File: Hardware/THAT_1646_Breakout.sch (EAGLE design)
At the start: 20 parts, among them IC2 THAT1646, J2 OUTPUT, J6 CHASSIS

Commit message: Routed board.
Worked through initial checklist.
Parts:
- removed H5, H6, H7, H8: STAND-OFF, SparkFun-Electromechanical:STAND-OFF
- added FD1, FD2: FIDUCIALUFIDUCIAL, SparkFun-Aesthetics:FIDUCIALUFIDUCIAL
- added LOGO1, LOGO2: SFE_LOGO_NAME.1_INCH, SparkFun-Aesthetics:SFE_LOGO_NAME.1_INCH
- added LOGO3: SFE_LOGO_FLAME.2_INCH, SparkFun-Aesthetics:SFE_LOGO_FLAME.2_INCH
- added LOGO4, LOGO5: OSHW-LOGOS, SparkFun-Aesthetics:OSHW-LOGOS
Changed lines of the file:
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@@
 <part name="IC2" library="that-ics" deviceset="THAT1646" device="" value="THAT1646"/>
 <part name="GND3" library="SparkFun-Aesthetics" deviceset="GND" device=""/>
-<part name="H5" library="SparkFun-Electromechanical" deviceset="STAND-OFF" device=""/>
-<part name="H6" library="SparkFun-Electromechanical" deviceset="STAND-OFF" device=""/>
-<part name="H7" library="SparkFun-Electromechanical" deviceset="STAND-OFF" device=""/>
-<part name="H8" library="SparkFun-Electromechanical" deviceset="STAND-OFF" device=""/>
 <part name="L1" library="SparkFun-Passives" deviceset="INDUCTOR" device="0603" value="27uH"/>
 <part name="L2" library="SparkFun-Passives" deviceset="INDUCTOR" device="0603" value="27uH"/>
@@
 <part name="SUPPLY14" library="SparkFun-Aesthetics" deviceset="VCC" device=""/>
 <part name="J6" library="SparkFun-Connectors" deviceset="M02" device="1X02_NO_SILK" value="CHASSIS"/>
+<part name="FD1" library="SparkFun-Aesthetics" deviceset="FIDUCIAL" device="UFIDUCIAL"/>
+<part name="FD2" library="SparkFun-Aesthetics" deviceset="FIDUCIAL" device="UFIDUCIAL"/>
+<part name="LOGO1" library="SparkFun-Aesthetics" deviceset="SFE_LOGO_NAME" device=".1_INCH"/>
+<part name="LOGO2" library="SparkFun-Aesthetics" deviceset="SFE_LOGO_NAME" device=".1_INCH"/>
+<part name="LOGO3" library="SparkFun-Aesthetics" deviceset="SFE_LOGO_FLAME" device=".2_INCH"/>
+<part name="LOGO4" library="SparkFun-Aesthetics" deviceset="OSHW-LOGO" device="S"/>
+<part name="LOGO5" library="SparkFun-Aesthetics" deviceset="OSHW-LOGO" device="S"/>
 </parts>
 <sheets>
@@
 <instance part="IC2" gate="G$1" x="71.12" y="111.76"/>
 <instance part="GND3" gate="1" x="63.5" y="114.3"/>
-<instance part="H5" gate="G$1" x="233.68" y="33.02"/>
-<instance part="H6" gate="G$1" x="233.68" y="30.48"/>
-<instance part="H7" gate="G$1" x="236.22" y="33.02"/>
-<instance part="H8" gate="G$1" x="236.22" y="30.48"/>
 <instance part="L1" gate="G$1" x="147.32" y="147.32" rot="R90"/>
 <instance part="L2" gate="G$1" x="147.32" y="139.7" rot="R90"/>
@@
 <instance part="SUPPLY14" gate="G$1" x="43.18" y="129.54"/>
 <instance part="J6" gate="G$1" x="210.82" y="129.54" rot="R180"/>
+<instance part="FD1" gate="G$1" x="246.38" y="20.32"/>
+<instance part="FD2" gate="G$1" x="246.38" y="17.78"/>
+<instance part="LOGO1" gate="G$1" x="187.96" y="35.56"/>
+<instance part="LOGO2" gate="G$1" x="187.96" y="35.56"/>
+<instance part="LOGO3" gate="G$1" x="180.34" y="38.1"/>
+<instance part="LOGO4" gate="G$1" x="157.48" y="45.72"/>
+<instance part="LOGO5" gate="G$1" x="157.48" y="45.72"/>
 </instances>
 <busses>

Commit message: Post-review updates.
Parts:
- removed C11, C12: 10uf, that-ics:PANA-EEE-1EA100NP
- removed LOGO5: OSHW-LOGOS, SparkFun-Aesthetics:OSHW-LOGOS
- added C3, C4: 10uf NP, that-ics:PANA-EEE-1EA100NP
- added FD3, FD4: FIDUCIALUFIDUCIAL, SparkFun-Aesthetics:FIDUCIALUFIDUCIAL
- added J1: (no value), SparkFun-Connectors:M04NO_SILK_ALL_ROUND
- added J3: CHASSIS, SparkFun-Connectors:M021X02_NO_SILK
- added J4: SN, SparkFun-Connectors:M01PTH_NO_SILK_YES_STOP
- added LOGO6: SFE_LOGO_FLAME.2_INCH, SparkFun-Aesthetics:SFE_LOGO_FLAME.2_INCH
- J5: value (none) -> TN; device SparkFun-Connectors:M04NO_SILK_ALL_ROUND -> SparkFun-Connectors:M01PTH_NO_SILK_YES_STOP
- J6: value CHASSIS -> RN; device SparkFun-Connectors:M021X02_NO_SILK -> SparkFun-Connectors:M01PTH_NO_SILK_YES_STOP
- JP1: value JUMPER-PAD-2-NC_BY_TRACE -> GND-JOIN
- L1, L2: PROD_ID (none) -> NDUC-12579
- LOGO1, LOGO2: value SFE_LOGO_NAME.1_INCH -> OSHW-LOGOS; device SparkFun-Aesthetics:SFE_LOGO_NAME.1_INCH -> SparkFun-Aesthetics:OSHW-LOGOS
- LOGO4: value OSHW-LOGOS -> SFE_LOGO_NAME.1_INCH; device SparkFun-Aesthetics:OSHW-LOGOS -> SparkFun-Aesthetics:SFE_LOGO_NAME.1_INCH
- renumbered C10 to C2, C7 to C6, C8 to C5, C9 to C1, IC2 to IC1, JP2 to JP1
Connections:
- new net N$1: J2.RING-NORM, J6.1
- new net N$2: J2.TIP-NORM, J5.1
- new net N$3: J2.EARTH-NORM, J4.1
- net GND: now also J1.1; no longer J5.1
- net GND-ISO: now also J3.1, J3.2; no longer J6.1, J6.2
- net N$10: now also C3.2, D1.COM; no longer C11.-, D2.COM
- net N$11: now also C4.2, D2.COM; no longer C12.-, D1.COM
- net N$13: now also C4.1; no longer C12.+
- net N$14: now also C3.1; no longer C11.+
- net N$16: now also J1.4; no longer J5.4
- net VCC: now also J1.3; no longer J5.3
- net VNEG: now also J1.2; no longer J5.2
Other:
- moved on the sheet: D1, D2, J2

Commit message: Updates from engineering checklist.
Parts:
- removed LOGO6: SFE_LOGO_FLAME.2_INCH, SparkFun-Aesthetics:SFE_LOGO_FLAME.2_INCH
- added LOGO5: SFE_LOGO_NAME.1_INCH, SparkFun-Aesthetics:SFE_LOGO_NAME.1_INCH
- D1, D2: value (none) -> BAV99
- J1: value (none) -> 1x4
- J2: value OUTPUT -> SN; device SparkFun-Connectors:AUDIO-JACK4-.25-HORIZ-TRS -> SparkFun-Connectors:M01PTH_NO_SILK_YES_STOP
- J4: value SN -> TN
- J5: value TN -> RN
- J6: value RN -> OUTPUT; device SparkFun-Connectors:M01PTH_NO_SILK_YES_STOP -> SparkFun-Connectors:AUDIO-JACK4-.25-HORIZ-TRS
- LOGO4: value SFE_LOGO_NAME.1_INCH -> SFE_LOGO_FLAME.2_INCH; device SparkFun-Aesthetics:SFE_LOGO_NAME.1_INCH -> SparkFun-Aesthetics:SFE_LOGO_FLAME.2_INCH
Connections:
- net GND-ISO: now also J6.EARTH; no longer J2.EARTH
- net N$1: now also J5.1, J6.RING-NORM; no longer J2.RING-NORM, J6.1
- net N$2: now also J4.1, J6.TIP-NORM; no longer J2.TIP-NORM, J5.1
- net N$3: now also J2.1, J6.EARTH-NORM; no longer J2.EARTH-NORM, J4.1
- net N$8: now also J6.TIP; no longer J2.TIP
- net N$9: now also J6.RING; no longer J2.RING
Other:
- note added: "J2, J4, J5 are normals of TRS connections. If jack is not present, they connect to their respective T/R/S connections. If jack is present, they float."
- moved on the sheet: J4, J5
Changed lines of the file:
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@@
 <parts>
 <part name="FRAME1" library="SparkFun-Aesthetics" deviceset="FRAME-LETTER" device=""/>
-<part name="J2" library="SparkFun-Connectors" deviceset="AUDIO-JACK4-.25-HORIZ-TRS" device="" value="OUTPUT"/>
+<part name="J6" library="SparkFun-Connectors" deviceset="AUDIO-JACK4-.25-HORIZ-TRS" device="" value="OUTPUT"/>
 <part name="SUPPLY3" library="SparkFun-Aesthetics" deviceset="VCC" device=""/>
 <part name="GND-ISO2" library="SparkFun-Aesthetics" deviceset="GND-ISO" device=""/>
@@
 <attribute name="PROD_ID" value="NDUC-12579"/>
 </part>
-<part name="D2" library="SparkFun-DiscreteSemi" deviceset="BAV99" device=""/>
-<part name="D1" library="SparkFun-DiscreteSemi" deviceset="BAV99" device=""/>
+<part name="D2" library="SparkFun-DiscreteSemi" deviceset="BAV99" device="" value="BAV99"/>
+<part name="D1" library="SparkFun-DiscreteSemi" deviceset="BAV99" device="" value="BAV99"/>
 <part name="SUPPLY6" library="SparkFun-Aesthetics" deviceset="VCC" device=""/>
 <part name="SUPPLY8" library="SparkFun-Aesthetics" deviceset="VCC" device=""/>
@@
 <part name="GND3" library="SparkFun-Aesthetics" deviceset="GND" device=""/>
 <part name="GND2" library="SparkFun-Aesthetics" deviceset="GND" device=""/>
-<part name="J1" library="SparkFun-Connectors" deviceset="M04" device="NO_SILK_ALL_ROUND"/>
+<part name="J1" library="SparkFun-Connectors" deviceset="M04" device="NO_SILK_ALL_ROUND" value="1x4"/>
 <part name="GND1" library="SparkFun-Aesthetics" deviceset="GND" device=""/>
 <part name="SUPPLY2" library="SparkFun-Aesthetics" deviceset="VNEG" device=""/>
 <part name="SUPPLY1" library="SparkFun-Aesthetics" deviceset="VCC" device=""/>
 <part name="J3" library="SparkFun-Connectors" deviceset="M02" device="1X02_NO_SILK" value="CHASSIS"/>
-<part name="FD1" library="SparkFun-Aesthetics" deviceset="FIDUCIAL" device="UFIDUCIAL"/>
-<part name="FD2" library="SparkFun-Aesthetics" deviceset="FIDUCIAL" device="UFIDUCIAL"/>
-<part name="LOGO4" library="SparkFun-Aesthetics" deviceset="SFE_LOGO_NAME" device=".1_INCH"/>
+<part name="FD3" library="SparkFun-Aesthetics" deviceset="FIDUCIAL" device="UFIDUCIAL"/>
+<part name="FD4" library="SparkFun-Aesthetics" deviceset="FIDUCIAL" device="UFIDUCIAL"/>
+<part name="LOGO5" library="SparkFun-Aesthetics" deviceset="SFE_LOGO_NAME" device=".1_INCH"/>
 <part name="LOGO3" library="SparkFun-Aesthetics" deviceset="SFE_LOGO_FLAME" device=".2_INCH"/>
 <part name="LOGO1" library="SparkFun-Aesthetics" deviceset="OSHW-LOGO" device="S"/>
 <part name="LOGO2" library="SparkFun-Aesthetics" deviceset="OSHW-LOGO" device="S"/>
-<part name="J4" library="SparkFun-Connectors" deviceset="M01" device="PTH_NO_SILK_YES_STOP" value="SN"/>
-<part name="J5" library="SparkFun-Connectors" deviceset="M01" device="PTH_NO_SILK_YES_STOP" value="TN"/>
-<part name="J6" library="SparkFun-Connectors" deviceset="M01" device="PTH_NO_SILK_YES_STOP" value="RN"/>
-<part name="LOGO6" library="SparkFun-Aesthetics" deviceset="SFE_LOGO_FLAME" device=".2_INCH"/>
-<part name="FD3" library="SparkFun-Aesthetics" deviceset="FIDUCIAL" device="UFIDUCIAL"/>
-<part name="FD4" library="SparkFun-Aesthetics" deviceset="FIDUCIAL" device="UFIDUCIAL"/>
+<part name="J2" library="SparkFun-Connectors" deviceset="M01" device="PTH_NO_SILK_YES_STOP" value="SN"/>
+<part name="J4" library="SparkFun-Connectors" deviceset="M01" device="PTH_NO_SILK_YES_STOP" value="TN"/>
+<part name="J5" library="SparkFun-Connectors" deviceset="M01" device="PTH_NO_SILK_YES_STOP" value="RN"/>
+<part name="LOGO4" library="SparkFun-Aesthetics" deviceset="SFE_LOGO_FLAME" device=".2_INCH"/>
+<part name="FD1" library="SparkFun-Aesthetics" deviceset="FIDUCIAL" device="UFIDUCIAL"/>
+<part name="FD2" library="SparkFun-Aesthetics" deviceset="FIDUCIAL" device="UFIDUCIAL"/>
 <part name="C3" library="that-ics" deviceset="PANA-EEE-1EA100NP" device="" value="10uf NP"/>
 <part name="C4" library="that-ics" deviceset="PANA-EEE-1EA100NP" device="" value="10uf NP"/>
@@
 <text x="7.62" y="177.8" size="2.54" layer="97" align="top-left">This board requires bipolar power,
  in the range from +/-5VDC to +/-20VDC.</text>
+<text x="182.88" y="99.06" size="2.1844" layer="97" font="vector" align="top-left">J2, J4, J5 are normals of
+TRS connections.  If jack
+is not present, they
+connect to their respective
+T/R/S connections.
+If jack is present, they float.</text>
 </plain>
 <instances>
 <instance part="FRAME1" gate="G$1" x="0" y="0"/>
 <instance part="FRAME1" gate="V" x="147.32" y="0"/>
-<instance part="J2" gate="G$1" x="236.22" y="144.78" rot="R180"/>
+<instance part="J6" gate="G$1" x="236.22" y="144.78" rot="R180"/>
 <instance part="SUPPLY3" gate="G$1" x="78.74" y="149.86"/>
 <instance part="GND-ISO2" gate="G$1" x="198.12" y="116.84"/>
@@
 <instance part="SUPPLY1" gate="G$1" x="43.18" y="129.54"/>
 <instance part="J3" gate="G$1" x="210.82" y="129.54" rot="R180"/>
-<instance part="FD1" gate="G$1" x="246.38" y="20.32"/>
-<instance part="FD2" gate="G$1" x="246.38" y="17.78"/>
-<instance part="LOGO4" gate="G$1" x="187.96" y="35.56"/>
+<instance part="FD3" gate="G$1" x="246.38" y="20.32"/>
+<instance part="FD4" gate="G$1" x="246.38" y="17.78"/>
+<instance part="LOGO5" gate="G$1" x="187.96" y="35.56"/>
 <instance part="LOGO3" gate="G$1" x="180.34" y="38.1"/>
 <instance part="LOGO1" gate="G$1" x="157.48" y="45.72"/>
 <instance part="LOGO2" gate="G$1" x="157.48" y="45.72"/>
-<instance part="J4" gate="G$1" x="203.2" y="167.64" rot="R270"/>
-<instance part="J5" gate="G$1" x="215.9" y="167.64" rot="R270"/>
-<instance part="J6" gate="G$1" x="228.6" y="167.64" rot="R270"/>
-<instance part="LOGO6" gate="G$1" x="180.34" y="38.1"/>
-<instance part="FD3" gate="G$1" x="243.84" y="20.32"/>
-<instance part="FD4" gate="G$1" x="243.84" y="17.78"/>
+<instance part="J2" gate="G$1" x="203.2" y="167.64" rot="R270"/>
+<instance part="J4" gate="G$1" x="215.9" y="167.64" rot="R270"/>
+<instance part="J5" gate="G$1" x="228.6" y="167.64" rot="R270"/>
+<instance part="LOGO4" gate="G$1" x="180.34" y="38.1"/>
+<instance part="FD1" gate="G$1" x="243.84" y="20.32"/>
+<instance part="FD2" gate="G$1" x="243.84" y="17.78"/>
 <instance part="C3" gate="G$1" x="93.98" y="139.7" rot="R90"/>
 <instance part="C4" gate="G$1" x="93.98" y="106.68" rot="R90"/>
@@
 <pinref part="GND-ISO2" gate="G$1" pin="GND-ISO"/>
 <wire x1="198.12" y1="119.38" x2="198.12" y2="124.46" width="0.1524" layer="91"/>
-<pinref part="J2" gate="G$1" pin="EARTH"/>
+<pinref part="J6" gate="G$1" pin="EARTH"/>
 <wire x1="198.12" y1="124.46" x2="198.12" y2="127" width="0.1524" layer="91"/>
 <wire x1="198.12" y1="127" x2="198.12" y2="129.54" width="0.1524" layer="91"/>
@@
 <segment>
 <pinref part="L2" gate="G$1" pin="2"/>
-<pinref part="J2" gate="G$1" pin="TIP"/>
+<pinref part="J6" gate="G$1" pin="TIP"/>
 <wire x1="154.94" y1="139.7" x2="177.8" y2="139.7" width="0.1524" layer="91"/>
 <pinref part="C5" gate="G$1" pin="1"/>
@@
 <net name="N$9" class="0">
 <segment>
-<pinref part="J2" gate="G$1" pin="RING"/>
+<pinref part="J6" gate="G$1" pin="RING"/>
 <wire x1="231.14" y1="147.32" x2="187.96" y2="147.32" width="0.1524" layer="91"/>
 <pinref part="L1" gate="G$1" pin="2"/>
@@
 <net name="N$1" class="0">
 <segment>
-<pinref part="J2" gate="G$1" pin="RING-NORM"/>
-<pinref part="J6" gate="G$1" pin="1"/>
+<pinref part="J6" gate="G$1" pin="RING-NORM"/>
+<pinref part="J5" gate="G$1" pin="1"/>
 <wire x1="231.14" y1="149.86" x2="228.6" y2="149.86" width="0.1524" layer="91"/>
 <wire x1="228.6" y1="149.86" x2="228.6" y2="160.02" width="0.1524" layer="91"/>
@@
 <net name="N$2" class="0">
 <segment>
-<pinref part="J2" gate="G$1" pin="TIP-NORM"/>
-<pinref part="J5" gate="G$1" pin="1"/>
+<pinref part="J6" gate="G$1" pin="TIP-NORM"/>
+<pinref part="J4" gate="G$1" pin="1"/>
 <wire x1="231.14" y1="144.78" x2="215.9" y2="144.78" width="0.1524" layer="91"/>
 <wire x1="215.9" y1="144.78" x2="215.9" y2="160.02" width="0.1524" layer="91"/>
@@
 <net name="N$3" class="0">
 <segment>
-<pinref part="J2" gate="G$1" pin="EARTH-NORM"/>
-<pinref part="J4" gate="G$1" pin="1"/>
+<pinref part="J6" gate="G$1" pin="EARTH-NORM"/>
+<pinref part="J2" gate="G$1" pin="1"/>
 <wire x1="231.14" y1="139.7" x2="203.2" y2="139.7" width="0.1524" layer="91"/>
 <wire x1="203.2" y1="139.7" x2="203.2" y2="160.02" width="0.1524" layer="91"/>

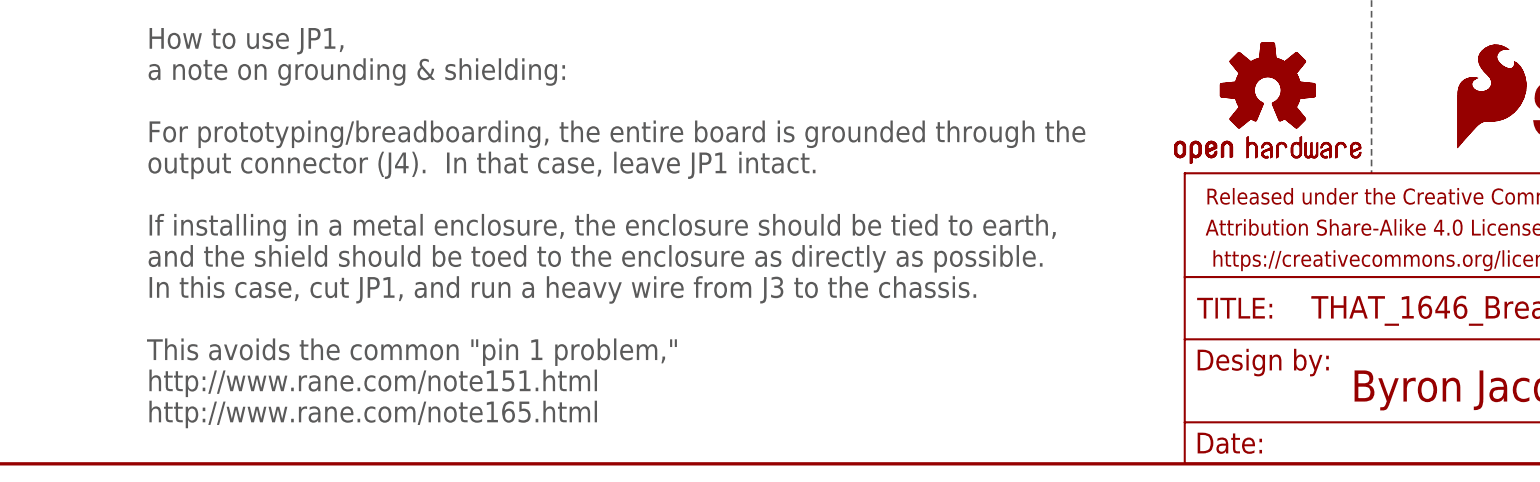
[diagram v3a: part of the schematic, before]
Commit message: Addressing Kade's checklist issues.
-Via under "THAT" in top silk
-Nixing "Toed"
-90-deg trace on bottom made 45.
-Moved chassis connection out from under TRS.
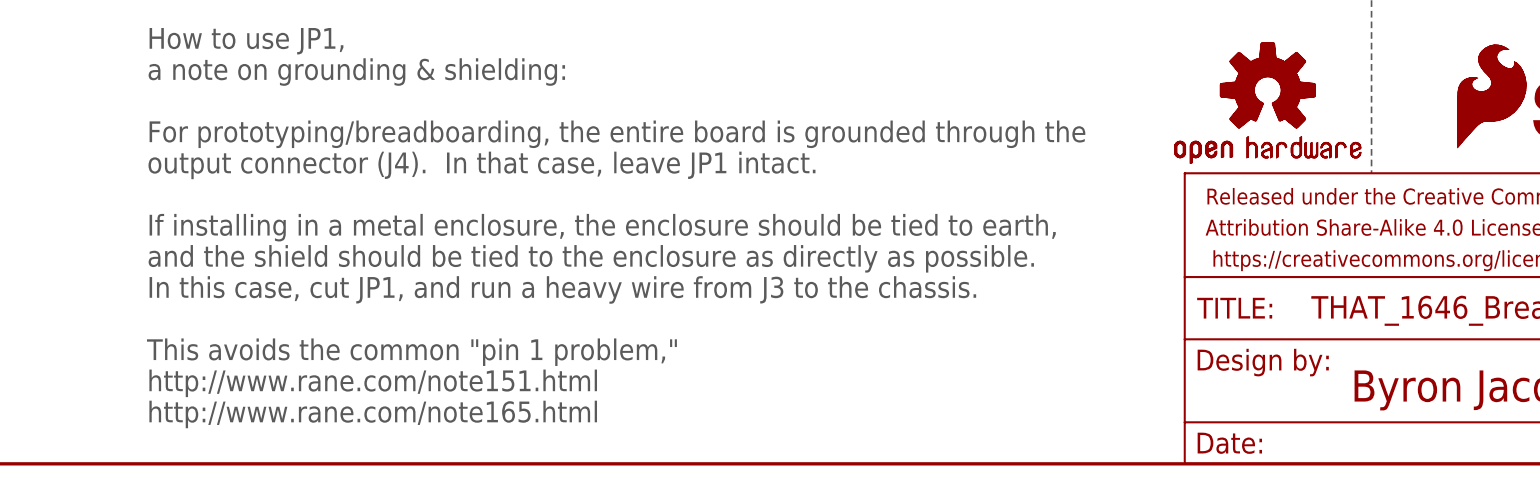
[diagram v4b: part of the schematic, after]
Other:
- note added: "How to use JP1, a note on grounding & shielding: For prototyping/breadboarding, the entire board is grounded through the output connector (J4). In that case, leave JP1 intact. If installing in a metal enclosure, the enclosure should be tied to earth, and the shield should be tied to the enclosure as directly as possible. In this case, cut JP1, and run a heavy wire from J3 to the chassis. This avo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"
- note removed: "How to use JP1, a note on grounding & shielding: For prototyping/breadboarding, the entire board is grounded through the output connector (J4). In that case, leave JP1 intact. If installing in a metal enclosure, the enclosure should be tied to earth, and the shield should be toed to the enclosure as directly as possible. In this case, cut JP1, and run a heavy wire from J3 to the chassis. This avo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"
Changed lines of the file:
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@@
 output connector (J4).  In that case, leave JP1 intact.
 If installing in a metal enclosure, the enclosure should be tied to earth,
-and the shield should be toed to the enclosure as directly as possible.
+and the shield should be tied to the enclosure as directly as possible.
 In this case, cut JP1, and run a heavy wire from J3 to the chassis.
 This avoids the common "pin 1 problem,"
